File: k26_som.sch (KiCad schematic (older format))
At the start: 37 parts, among them J6 22-23-2021, M1 XILINX-KRIA-K26, Q6 PJA3441, Q7 DTC014TEBTL

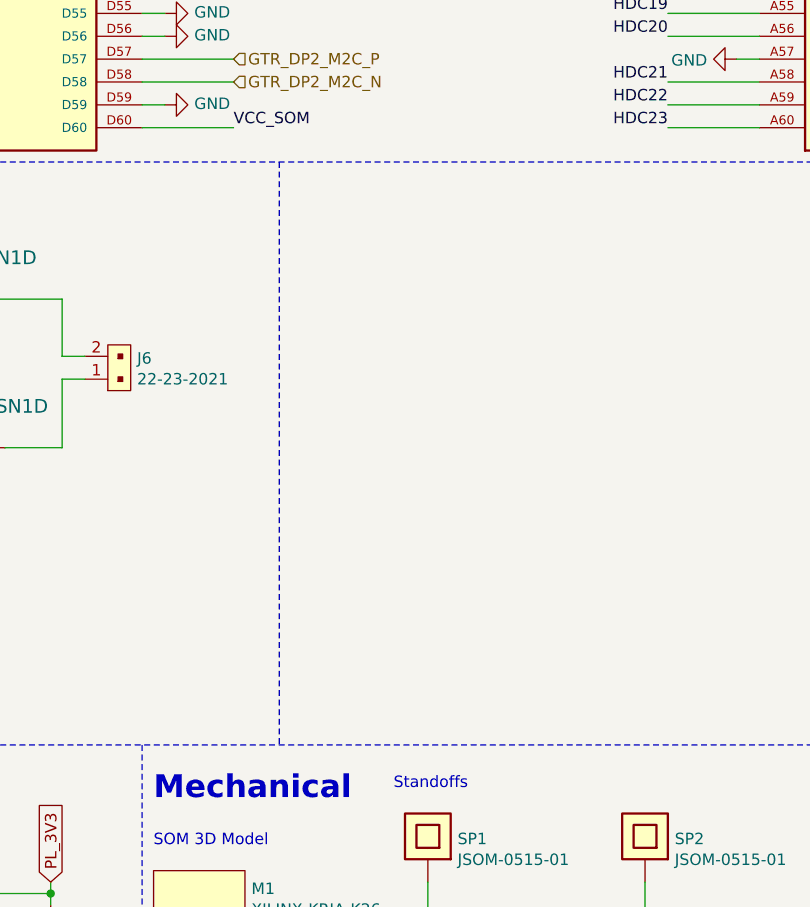
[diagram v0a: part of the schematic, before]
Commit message: Added Shutdown pulldown on the Schematic
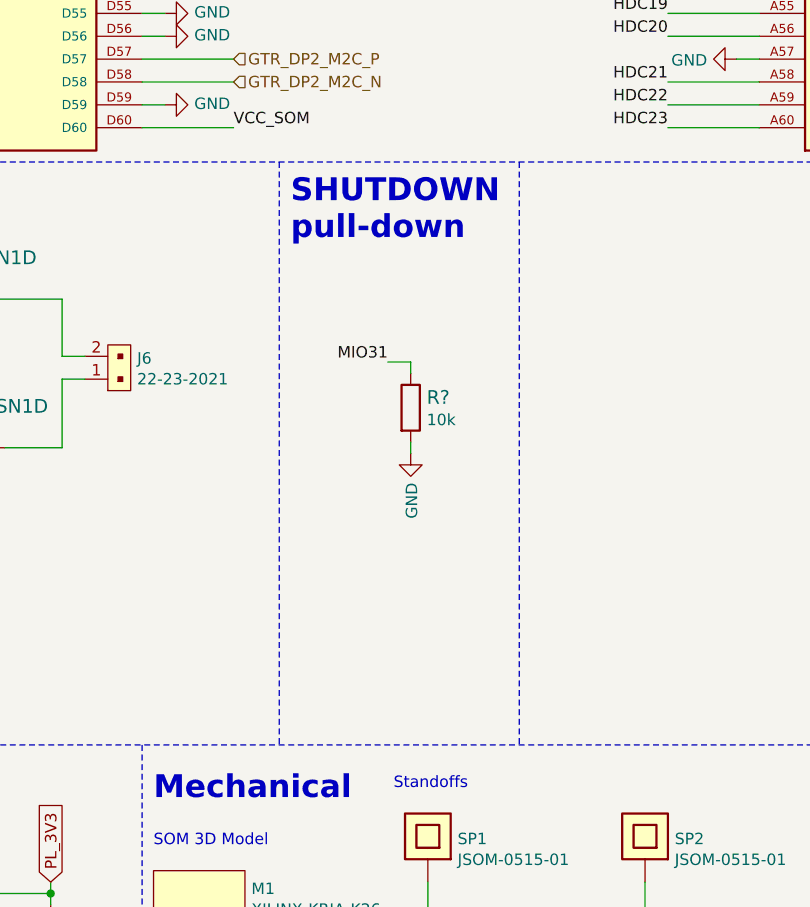
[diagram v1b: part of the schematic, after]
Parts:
- added R?: R_10k_0402, antmicro-footprints:0402-res, symbol antmicroResistors0402:R_10k_0402
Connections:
- net GND: now also R?.2
- new net MIO31: R?.1
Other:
- note added: "SHUTDOWN \npull-down"
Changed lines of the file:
@@
 Text GLabel 3650 7750 0    50   Input ~ 0
 USB_5V
+$Comp
+L antmicroResistors0402:R_10k_0402 R?
+U 1 1 62B7DD1C
+P 8175 8225
+F 0 "R?" V 8130 8295 60  0000 L CNN
+F 1 "R_10k_0402" H 8175 8075 60  0001 C CNN
+F 2 "antmicro-footprints:0402-res" H 8375 8425 60  0001 L CNN
+F 3 "" H 8175 8225 50  0001 C CNN
+F 4 "VISHAY" H 8375 8625 60  0001 L CNN "Manufacturer"
+F 5 "CRCW040210K0FKEDHP" H 8375 8525 60  0001 L CNN "MPN"
+F 6 "10k" V 8228 8295 50  0000 L CNN "Val"
+	1    8175 8225
+	0    1    1    0
+$EndComp
+$Comp
+L kria-k26-devboard:GND #PWR?
+U 1 1 62B8228F
+P 8175 8425
+F 0 "#PWR?" H 8175 8175 50  0001 C CNN
+F 1 "GND" V 8180 8297 50  0000 R CNN
+F 2 "" H 8175 8425 50  0001 C CNN
+F 3 "" H 8175 8425 50  0001 C CNN
+	1    8175 8425
+	1    0    0    -1
+$EndComp
+Wire Wire Line
+	8175 8425 8175 8375
+Text Label 8075 8025 2    50   ~ 0
+MIO31
+Wire Wire Line
+	8075 8025 8175 8025
+Wire Wire Line
+	8175 8025 8175 8075
+Text Notes 7650 7500 0    100  ~ 20
+SHUTDOWN \npull-down
+Wire Notes Line
+	8650 7150 8650 9700
 Wire Bus Line
 	3950 4350 3950 4500

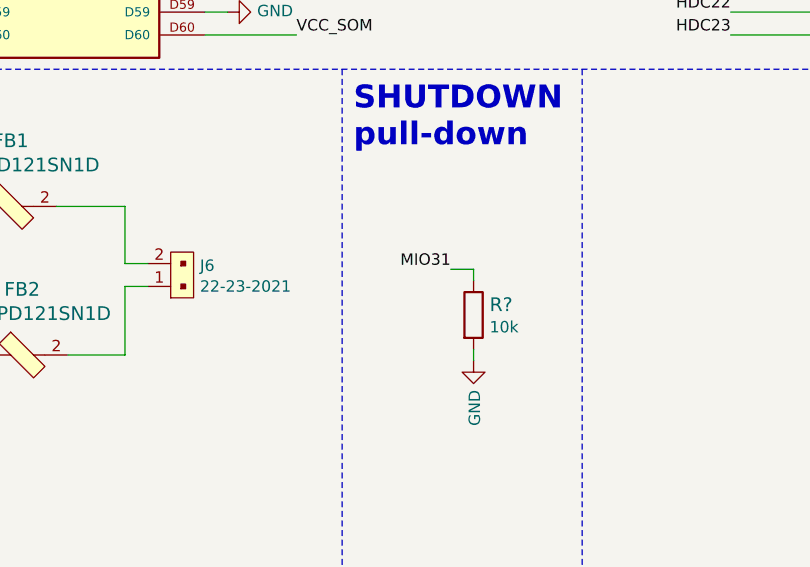
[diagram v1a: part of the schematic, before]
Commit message: Added Shutdown pulldown on the PCB, re-tuned DP aux signals after the change
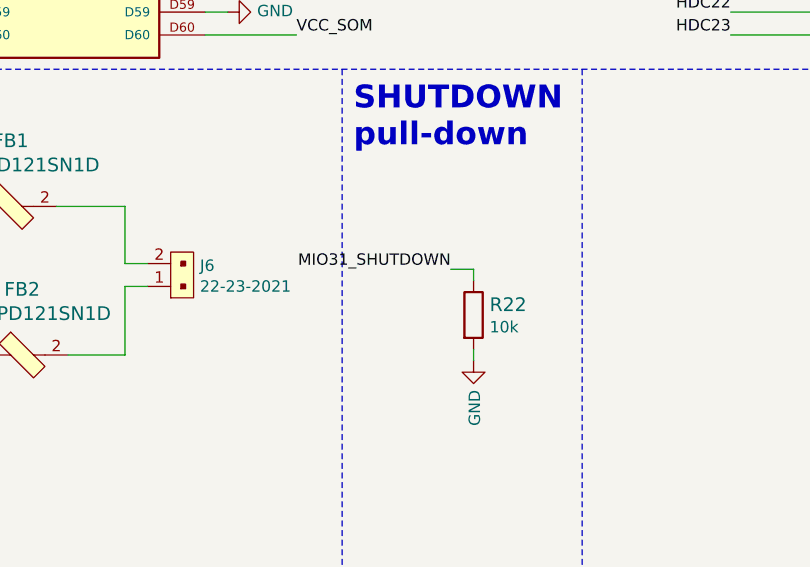
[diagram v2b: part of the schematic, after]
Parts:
- gave numbers to parts that had none: 1
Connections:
- net MIO31 is gone; now on net MIO31_SHUTDOWN: R22.1
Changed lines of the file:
@@
 USB_5V
 $Comp
-L antmicroResistors0402:R_10k_0402 R?
+L antmicroResistors0402:R_10k_0402 R22
 U 1 1 62B7DD1C
 P 8175 8225
-F 0 "R?" V 8130 8295 60  0000 L CNN
+F 0 "R22" V 8130 8295 60  0000 L CNN
 F 1 "R_10k_0402" H 8175 8075 60  0001 C CNN
 F 2 "antmicro-footprints:0402-res" H 8375 8425 60  0001 L CNN
@@
 $EndComp
 $Comp
-L kria-k26-devboard:GND #PWR?
+L kria-k26-devboard:GND #PWR0404
 U 1 1 62B8228F
 P 8175 8425
-F 0 "#PWR?" H 8175 8175 50  0001 C CNN
+F 0 "#PWR0404" H 8175 8175 50  0001 C CNN
 F 1 "GND" V 8180 8297 50  0000 R CNN
 F 2 "" H 8175 8425 50  0001 C CNN
@@
 	8175 8425 8175 8375
 Text Label 8075 8025 2    50   ~ 0
-MIO31
+MIO31_SHUTDOWN
 Wire Wire Line
 	8075 8025 8175 8025

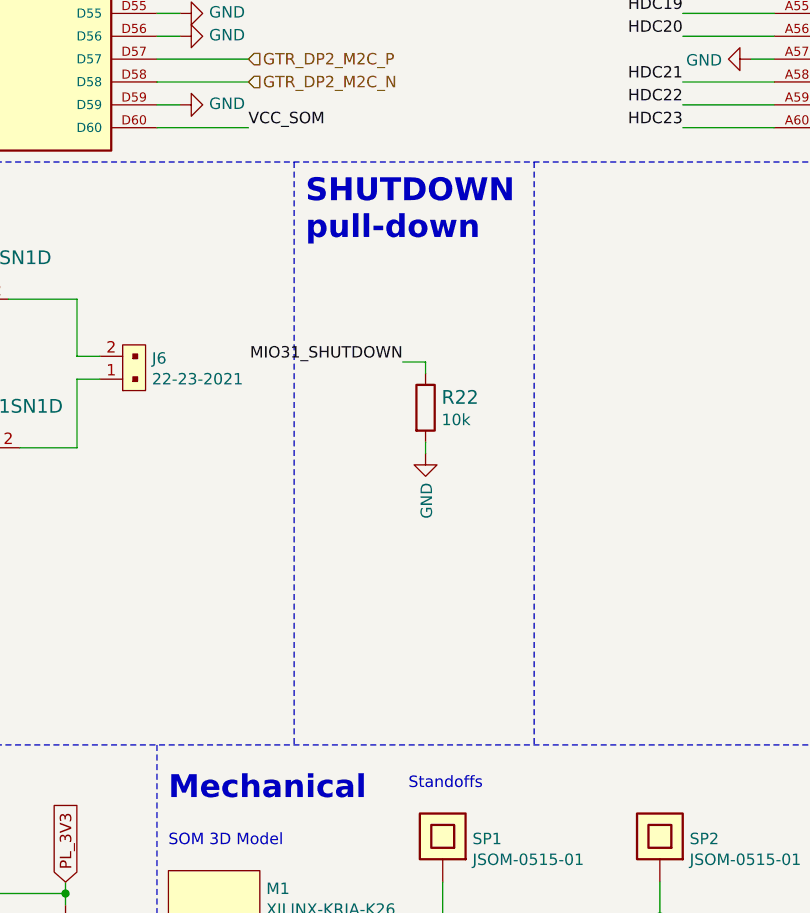
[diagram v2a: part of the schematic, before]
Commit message: Fixed wrong footprint assigment for L4 and L7, PCB changed to fit proper inductor footprints. Fixed R22 missing lib
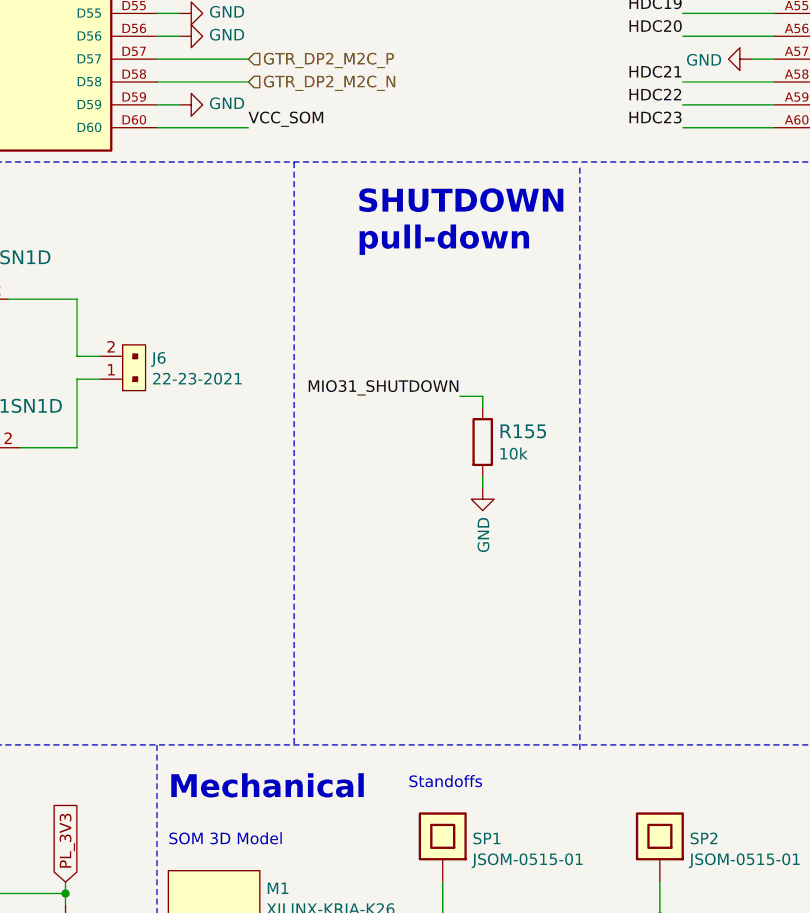
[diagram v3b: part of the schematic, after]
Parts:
- renumbered R22 to R155
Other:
- moved on the sheet: R155
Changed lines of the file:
@@
 USB_5V
 $Comp
-L antmicroResistors0402:R_10k_0402 R22
+L antmicroResistors0402:R_10k_0402 R155
 U 1 1 62B7DD1C
-P 8175 8225
-F 0 "R22" V 8130 8295 60  0000 L CNN
-F 1 "R_10k_0402" H 8175 8075 60  0001 C CNN
-F 2 "antmicro-footprints:0402-res" H 8375 8425 60  0001 L CNN
-F 3 "" H 8175 8225 50  0001 C CNN
-F 4 "VISHAY" H 8375 8625 60  0001 L CNN "Manufacturer"
-F 5 "CRCW040210K0FKEDHP" H 8375 8525 60  0001 L CNN "MPN"
-F 6 "10k" V 8228 8295 50  0000 L CNN "Val"
-	1    8175 8225
+P 8425 8375
+F 0 "R155" V 8380 8445 60  0000 L CNN
+F 1 "R_10k_0402" H 8425 8225 60  0001 C CNN
+F 2 "antmicro-footprints:0402-res" H 8625 8575 60  0001 L CNN
+F 3 "" H 8425 8375 50  0001 C CNN
+F 4 "VISHAY" H 8625 8775 60  0001 L CNN "Manufacturer"
+F 5 "CRCW040210K0FKEDHP" H 8625 8675 60  0001 L CNN "MPN"
+F 6 "10k" V 8478 8445 50  0000 L CNN "Val"
+	1    8425 8375
 	0    1    1    0
 $EndComp
@@
 L kria-k26-devboard:GND #PWR0404
 U 1 1 62B8228F
-P 8175 8425
-F 0 "#PWR0404" H 8175 8175 50  0001 C CNN
-F 1 "GND" V 8180 8297 50  0000 R CNN
-F 2 "" H 8175 8425 50  0001 C CNN
-F 3 "" H 8175 8425 50  0001 C CNN
-	1    8175 8425
+P 8425 8575
+F 0 "#PWR0404" H 8425 8325 50  0001 C CNN
+F 1 "GND" V 8430 8447 50  0000 R CNN
+F 2 "" H 8425 8575 50  0001 C CNN
+F 3 "" H 8425 8575 50  0001 C CNN
+	1    8425 8575
 	1    0    0    -1
 $EndComp
 Wire Wire Line
-	8175 8425 8175 8375
-Text Label 8075 8025 2    50   ~ 0
+	8425 8575 8425 8525
+Text Label 8325 8175 2    50   ~ 0
 MIO31_SHUTDOWN
 Wire Wire Line
-	8075 8025 8175 8025
+	8325 8175 8425 8175
 Wire Wire Line
-	8175 8025 8175 8075
-Text Notes 7650 7500 0    100  ~ 20
+	8425 8175 8425 8225
+Text Notes 7875 7550 0    100  ~ 20
 SHUTDOWN \npull-down
 Wire Notes Line
-	8650 7150 8650 9700
+	8850 7175 8850 9725
 Wire Bus Line
 	3950 4350 3950 4500
